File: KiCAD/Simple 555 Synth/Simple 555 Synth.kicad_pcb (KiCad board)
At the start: 2 copper layers, 10 parts, among them P1 PWR_5v, P4 EasyLAB_LOGO, U1 555-timer, U2 555-timer

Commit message: schema en printplaat Versie 20180625 0.6
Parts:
- removed P1: PWR_5v, Socket_Strips:Socket_Strip_Angled_1x02
- removed SP1: Luidspreker, Buzzers_Beepers:Buzzer_12x9.5RM7.6
- added C2: 10uF, Capacitors_ThroughHole:C_Radial_D5_L11_P2.5, F.Cu at (66.5, 53.4)
- added D1: LED1, LEDs:LED_D3.0mm, F.Cu at (35.7, 48.1)
- added D2: LED2, LEDs:LED_D3.0mm, F.Cu at (87.5, 29.9)
- added J1: Stroom, Socket_Strips:Socket_Strip_Angled_1x02, F.Cu at (34.3, 39.2)
- added J2: CapacitorInput, Socket_Strips:Socket_Strip_Straight_1x02, F.Cu at (79.7, 34.3)
- added J3: geluid_uit, footprints:Tayda_3.5mm_stereo_TRS_jack_A-853, F.Cu at (80.9, 61.3)
- added R4: R470K, w_pth_resistors:RC07, F.Cu at (48.0, 25.4)
- added R5: R_PHOTO2, w_pth_resistors:RC07, F.Cu at (71.1, 21.9)
- added R6: R1K, w_pth_resistors:RC07, F.Cu at (64.3, 63.8)
- added R7: R1K, w_pth_resistors:RC07, F.Cu at (47.3, 59.9)
- added R8: R1k, w_pth_resistors:RC07, F.Cu at (101.0, 38.0)
- added RV1: POT_50k, w_pth_resistors:trimmer_ecp_ca9-v10, F.Cu at (98.5, 60.6)
- added U3: LM358, w_pth_circuits:dil_8-300_socket, F.Cu at (82.9, 42.8)
- C1: value 01.uF -> 0.1uF; footprint Capacitors_ThroughHole:C_Disc_D3_P2.5 -> Capacitors_ThroughHole:C_Radial_D5_L11_P2.5
- C3: footprint Capacitors_ThroughHole:C_Radial_D6.3_L11.2_P2.5 -> Capacitors_ThroughHole:C_Radial_D5_L11_P2.5
- R1: value R100k -> R470K
- R2: value R1k -> R_PHOTO1
- R3: value R50k -> R1K
- U1, U2: value 555-timer -> NE555
- moved C3 39.7 mm to (93.1, 45.8)
- moved R2 38.7 mm to (70.3, 29.8)
- moved R1 30.6 mm to (48.0, 32.2)
- moved P4 22.0 mm to (69.1, 40.4)
- moved U2 18.0 mm to (65.3, 42.5)
- moved C1 17.9 mm to (32.9, 57.3)
- moved U1 17.8 mm to (48.6, 42.6)
- moved R3 11.0 mm to (47.7, 53.6), turned to 180 degrees
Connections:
- C1 pad 1: /TRG -> /TRG1
- C1 pad 2: /DIS -> /TRG1
- C3 pad 1: /SPKR -> Net-(C3-Pad1)
- R1 pad 1: /DIS2 -> /RST2
- R1 pad 2: /VSS -> /RST1
- R2 pad 1: /THR -> /RST1
- R2 pad 2: /DIS -> /RST1
- R3 pad 1: /DIS -> /geluid1
- R3 pad 2: /VSS -> Net-(D1-Pad2)
- U1 pad 1: /VSS -> /TRG1
- U1 pad 2: /TRG -> /TRG1
- U1 pad 3: /OUT -> /geluid1
- U1 pad 4: /OUT -> /RST1
- U1 pad 6: /THR -> /RST1
- U1 pad 7: /DIS -> /RST1
- U1 pad 8: /RESET2 -> /RST2
- U2 pad 1: /VSS -> /TRG1
- U2 pad 2: /OUT -> /geluid1
- U2 pad 3: /SPKR -> Net-(C2-Pad1)
- U2 pad 4: /RESET2 -> /RST2
- U2 pad 6: /DIS2 -> Net-(R5-Pad2)
- U2 pad 7: /DIS2 -> /Cap+
- U2 pad 8: /RESET2 -> /RST2
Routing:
- net /TRG1: track 0.00 -> 145.5 mm
- net /RST2: track 0.00 -> 75.2 mm
- net /RST1: track 0.00 -> 43.8 mm
- net Net-(J3-Pad1): track 0.00 -> 37.5 mm
- net /Cap+: track 0.00 -> 34.8 mm
- net Net-(R6-Pad1): track 0.00 -> 28.9 mm
- net /geluid1: track 0.00 -> 25.3 mm
- net Net-(R5-Pad2): track 0.00 -> 21.9 mm
- net Net-(C3-Pad2): track 0.00 -> 15.7 mm
- net Net-(C2-Pad2): track 0.00 -> 13.4 mm
- net Net-(D2-Pad2): track 0.00 -> 11.3 mm
- net Net-(C3-Pad1): track 0.00 -> 9.56 mm
- net Net-(C2-Pad1): track 0.00 -> 7.26 mm
- net Net-(D1-Pad2): track 0.00 -> 5.84 mm
- added copper zone on B.Cu, net (none)
- added copper zone on F.Cu, net (none)
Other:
- board outline added: 80.9 x 51.8 mm
- net class Default: trace_width 0.25 -> 0.35
- board text added: "Atari Punk Console Versie 20180625 0.6"
- board text added: "Door: Michiel Erasmus http://easylab4kids.nl"

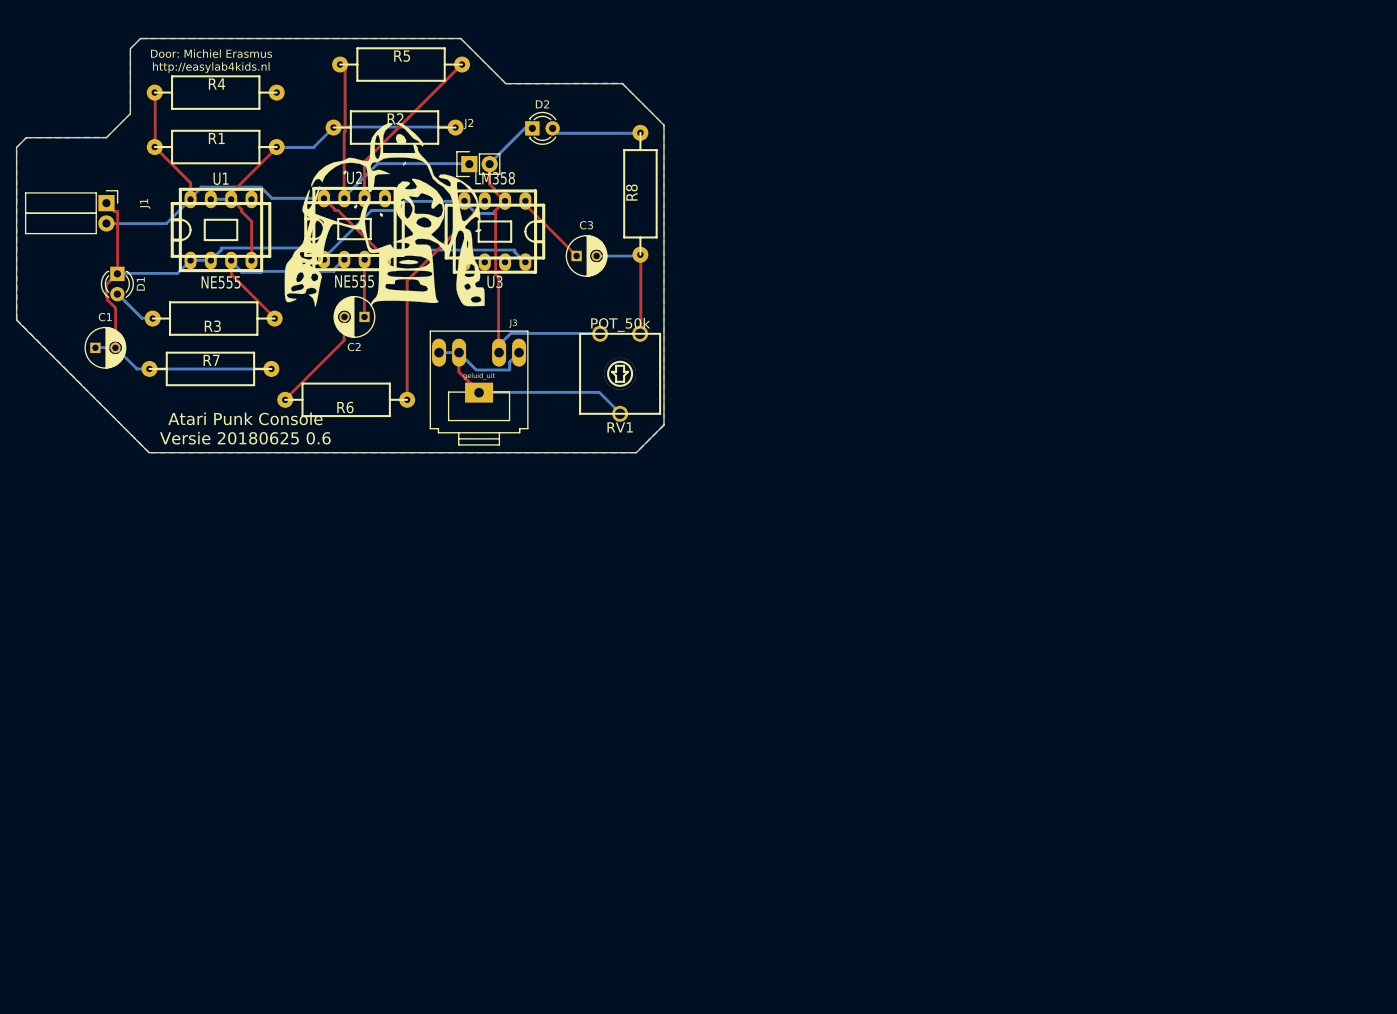
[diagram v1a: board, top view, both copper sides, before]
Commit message: Printplaat Versie 20180627 0.6
silkscreen teksten toegevoegd
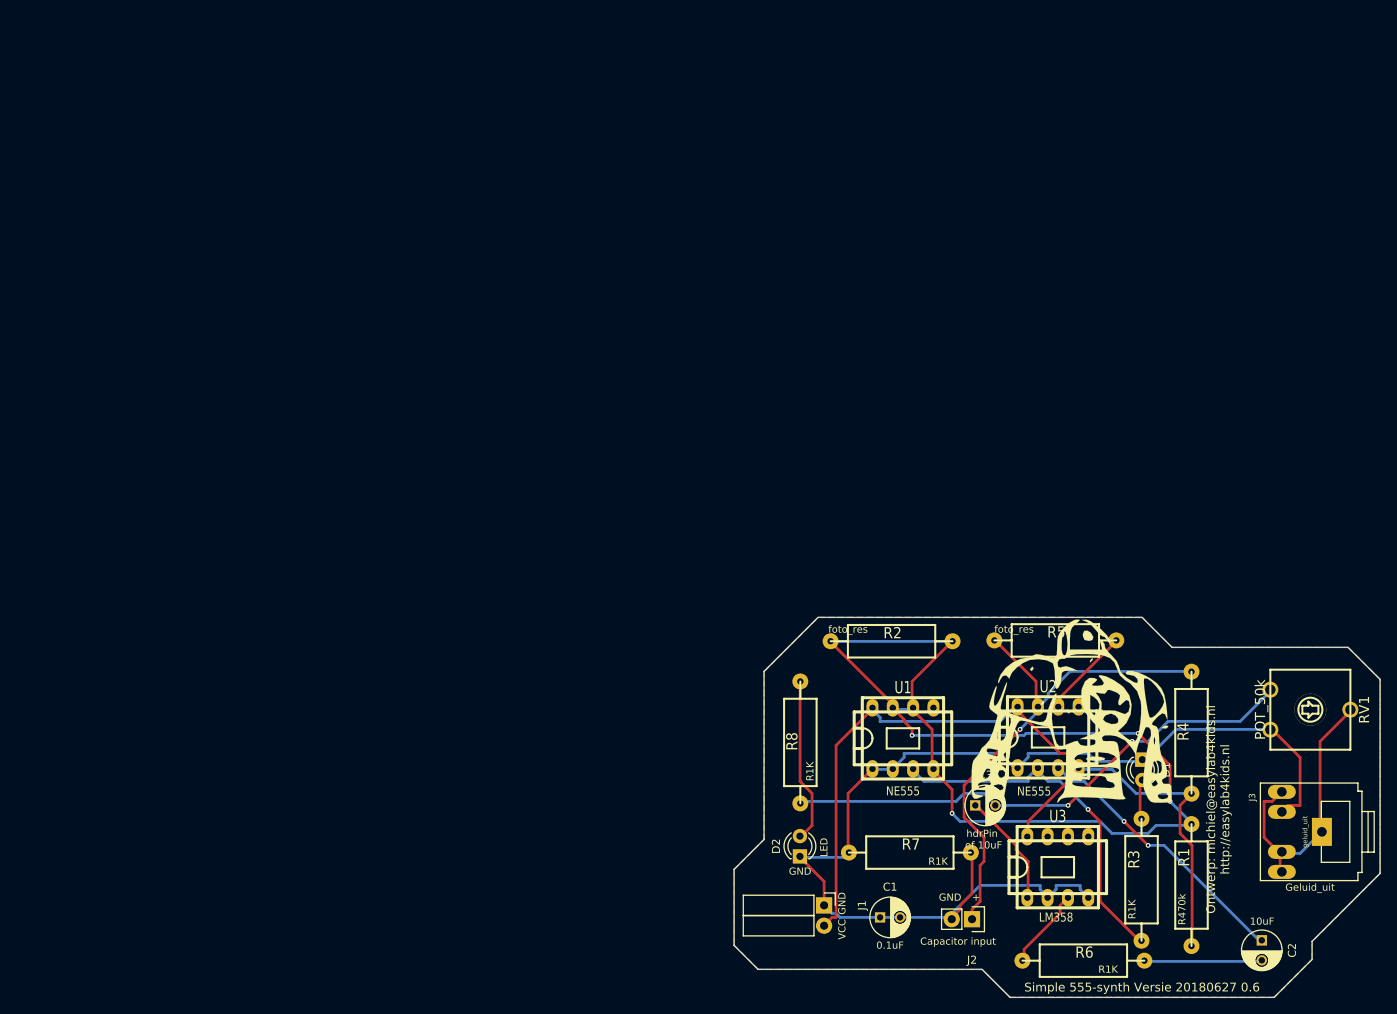
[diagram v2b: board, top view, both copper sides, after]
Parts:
- moved R1 152.9 mm to (169.9, 124.5), turned to 90 degrees
- moved R4 145.9 mm to (169.9, 105.4), turned to 90 degrees
- moved D1 141.8 mm to (163.8, 108.8)
- moved C2 136.6 mm to (178.7, 131.4), turned to 270 degrees
- moved R3 135.5 mm to (163.7, 123.8), turned to 90 degrees
- moved J1 125.5 mm to (124.0, 127.0)
- moved C1 121.2 mm to (131.0, 128.5)
- moved J3 118.1 mm to (184.6, 117.8), turned to 270 degrees
- moved R6 115.8 mm to (156.4, 133.9), turned to 0 degrees
- moved J2 113.4 mm to (142.5, 128.7), turned to 180 degrees
- moved R5 109.0 mm to (152.9, 93.9)
- moved U2 107.5 mm to (152.0, 106.0)
- moved U1 106.3 mm to (133.9, 106.1)
- moved R7 106.3 mm to (134.7, 120.4)
- moved U3 106.1 mm to (153.2, 122.2), turned to 0 degrees
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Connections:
- net /RST2 renamed /VCC
- net /TRG1 renamed GND
- J2 pad 1: /Cap+ -> /cap1
- R1 pad 2: /RST1 -> Net-(R1-Pad2)
- R2 pad 1: /RST1 -> Net-(R1-Pad2)
- R2 pad 2: /RST1 -> Net-(R2-Pad2)
- R4 pad 2: (no net) -> /cap1
- R5 pad 1: /Cap+ -> /cap1
- U1 pad 4: /RST1 -> Net-(R2-Pad2)
- U1 pad 6: /RST1 -> Net-(R2-Pad2)
- U1 pad 7: /RST1 -> Net-(R1-Pad2)
- U2 pad 7: /Cap+ -> /cap1
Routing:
- net Net-(R1-Pad2): track 0.00 -> 108.3 mm, vias 0 -> 4
- net /cap1: track 0.00 -> 64.6 mm, vias 0 -> 1
- net Net-(C3-Pad2): track 15.7 -> 66.7 mm, vias 0 -> 2
- net /RST1: track 43.8 -> 0.00 mm
- net /Cap+: track 34.8 -> 0.00 mm
- net /VCC: track 75.2 -> 109.3 mm
- net Net-(C2-Pad1): track 7.26 -> 34.7 mm, vias 0 -> 2
- net Net-(R2-Pad2): track 0.00 -> 26.8 mm
- net /geluid1: track 25.3 -> 45.7 mm, vias 0 -> 1
- net Net-(R6-Pad1): track 28.9 -> 10.5 mm
- net Net-(R5-Pad2): track 21.9 -> 11.3 mm
- net Net-(D2-Pad2): track 11.3 -> 20.9 mm
- net Net-(C3-Pad1): track 9.56 -> 14.4 mm
- net Net-(C2-Pad2): track 13.4 -> 14.8 mm
- net GND: track 145.5 -> 144.7 mm
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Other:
- board size 80.9 x 51.8 mm -> 80.8 x 47.5 mm
- board text added: "+"
- board text added: "0.1uF"
- board text added: "10uF"
- board text added: "Capacitor input"
- board text added: "En hoor jy die magtige dreuning? Oor die veld kom dit wyd gesweef: die lied van 'n volk se ontwaking wat harte laat sidder en beef. Van Kaapland tot bo in die Noorde rys dawerend luid die akkoorde: Dit is die LIED van Jong Suid-Afrika"
- board text added: "GND"
- board text added: "Geluid_uit"
- board text added: "LED"
- board text added: "Ontwerp: michiel@easylab4kids.nl http://easylab4kids.nl"
- board text added: "R1K"
- board text added: "R470k"
- board text added: "Simple 555-synth Versie 20180627 0.6"
- board text added: "VCC"
- board text added: "foto_res"
- board text added: "hdrPin of 10uF"
- board text removed: "Atari Punk Console Versie 20180625 0.6"
- board text removed: "Door: Michiel Erasmus http://easylab4kids.nl"
